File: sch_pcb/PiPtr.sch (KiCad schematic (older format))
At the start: 61 parts, among them J101 GLOBAL_LINK_LEFT, J102 GLOBAL_LINK_RIGHT, J107 RASPBERRY_PI, J111 FP_PIXEL, J112 AM2302, Q101 BSS138, Q102 BSS138, Q103 BSS138, Q104 BSS138, Q105 BSS138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

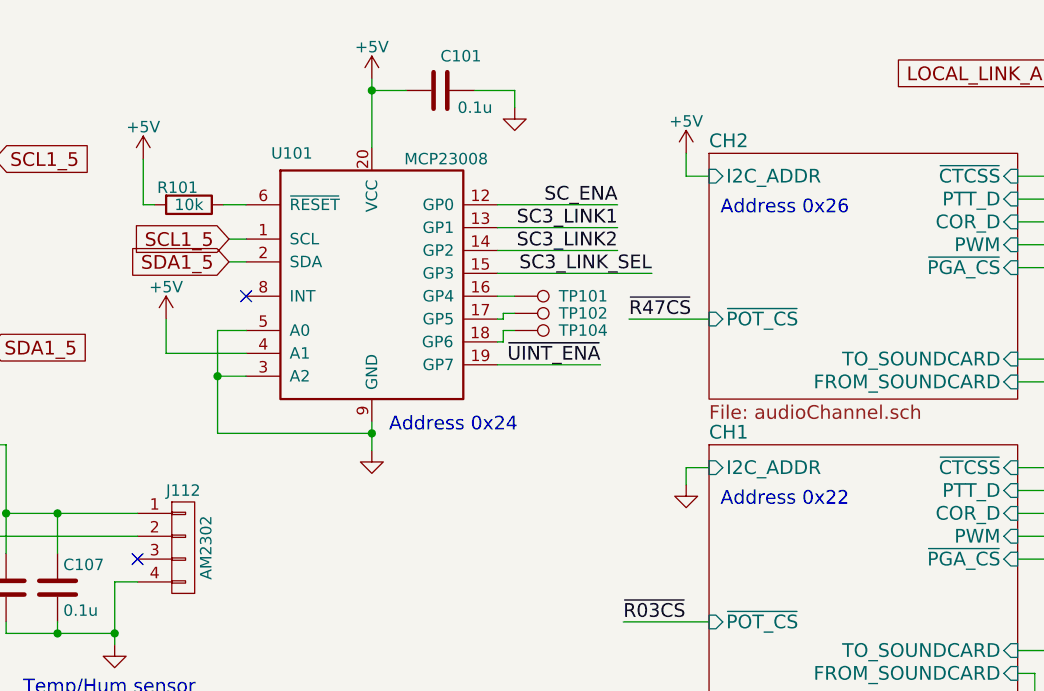
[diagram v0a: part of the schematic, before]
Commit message: Add files via upload
Fix i2c addressing
Change footprint for LDR
Move connectors for temp/hum sensor and rtc so they won't hit the Pi
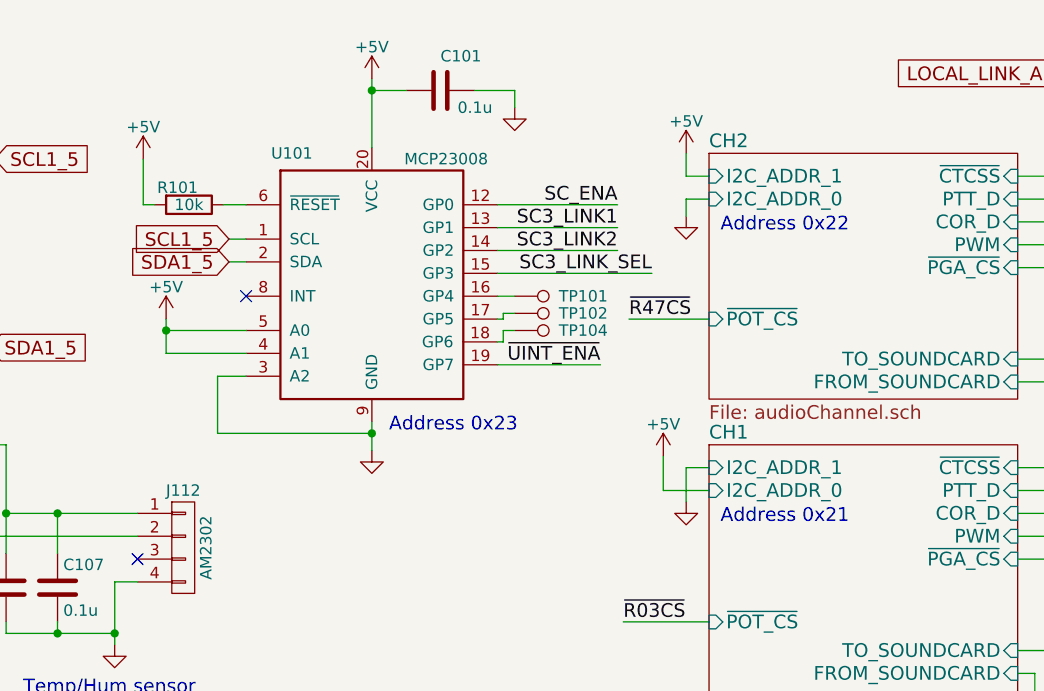
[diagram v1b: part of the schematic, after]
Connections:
- net +5V: now also U101.5 (A0)
- net GND: no longer U101.5 (A0)
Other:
- note added: "Address 0x21"
- note added: "Address 0x23"
- note removed: "Address 0x24"
- note removed: "Address 0x26"
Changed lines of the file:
@@
 F7 "TO_SOUNDCARD" I R 6400 3300 60
 F8 "FROM_SOUNDCARD" I R 6400 3400 60
-F9 "I2C_ADDR" I L 5050 2500 60
-F10 "~POT_CS" I L 5050 3175 60
+F9 "~POT_CS" I L 5050 3175 60
+F10 "I2C_ADDR_1" I L 5050 2500 60
+F11 "I2C_ADDR_0" I L 5050 2600 60
 $EndSheet
 $Sheet
@@
 F7 "TO_SOUNDCARD" I R 6400 2025 60
 F8 "FROM_SOUNDCARD" I R 6400 2125 60
-F9 "I2C_ADDR" I L 5050 1225 60
-F10 "~POT_CS" I L 5050 1850 60
+F9 "~POT_CS" I L 5050 1850 60
+F10 "I2C_ADDR_1" I L 5050 1225 60
+F11 "I2C_ADDR_0" I L 5050 1325 60
 $EndSheet
 $Sheet
@@
 L GND #PWR0128
 U 1 1 596A5C0A
-P 4950 2575
-F 0 "#PWR0128" H 4950 2325 50  0001 C CNN
-F 1 "GND" H 4950 2425 50  0001 C CNN
-F 2 "" H 4950 2575 50  0001 C CNN
-F 3 "" H 4950 2575 50  0001 C CNN
-	1    4950 2575
+P 4950 2650
+F 0 "#PWR0128" H 4950 2400 50  0001 C CNN
+F 1 "GND" H 4950 2500 50  0001 C CNN
+F 2 "" H 4950 2650 50  0001 C CNN
+F 3 "" H 4950 2650 50  0001 C CNN
+	1    4950 2650
 	1    0    0    -1
 $EndComp
@@
 	1    0    0    -1
 $EndComp
-Text Notes 5100 1400 0    60   ~ 0
-Address 0x26
+Text Notes 5100 1475 0    60   ~ 0
+Address 0x22
 Text Label 7875 3025 0    60   ~ 0
 PIXEL_33
@@
 Text GLabel 1900 1975 2    60   Input ~ 0
 SDA1_5
-Text Notes 5100 2675 0    60   ~ 0
-Address 0x22
+Text Notes 5100 2750 0    60   ~ 0
+Address 0x21
 Wire Wire Line
 	4950 1125 4950 1225
@@
 	5050 2500 4950 2500
 Wire Wire Line
-	4950 2500 4950 2575
+	4950 2500 4950 2650
 $Comp
 L R R101
@@
 	2950 1500 3025 1500
 Wire Wire Line
-	2900 1900 2900 2350
-Wire Wire Line
 	2900 2350 3575 2350
 Wire Wire Line
@@
 $EndComp
 Text Notes 3650 2350 0    60   ~ 0
-Address 0x24
+Address 0x23
 Wire Wire Line
 	8775 4075 8125 4075
@@
 Wire Wire Line
 	2675 1850 2675 2000
-Wire Wire Line
-	2900 1900 3025 1900
-Connection ~ 2900 2100
+$Comp
+L +5V #PWR?
+U 1 1 59C8550D
+P 4850 2450
+F 0 "#PWR?" H 4850 2300 50  0001 C CNN
+F 1 "+5V" H 4850 2590 50  0000 C CNN
+F 2 "" H 4850 2450 50  0001 C CNN
+F 3 "" H 4850 2450 50  0001 C CNN
+	1    4850 2450
+	1    0    0    -1
+$EndComp
+Wire Wire Line
+	4850 2450 4850 2600
+Wire Wire Line
+	4850 2600 5050 2600
+Wire Wire Line
+	5050 1325 4950 1325
+Wire Wire Line
+	4950 1325 4950 1400
+$Comp
+L GND #PWR?
+U 1 1 59C85DDE
+P 4950 1400
+F 0 "#PWR?" H 4950 1150 50  0001 C CNN
+F 1 "GND" H 4950 1250 50  0001 C CNN
+F 2 "" H 4950 1400 50  0001 C CNN
+F 3 "" H 4950 1400 50  0001 C CNN
+	1    4950 1400
+	1    0    0    -1
+$EndComp
+Wire Wire Line
+	3025 1900 2675 1900
+Connection ~ 2675 1900
+Wire Wire Line
+	2900 2100 2900 2350
 $EndSCHEMATC

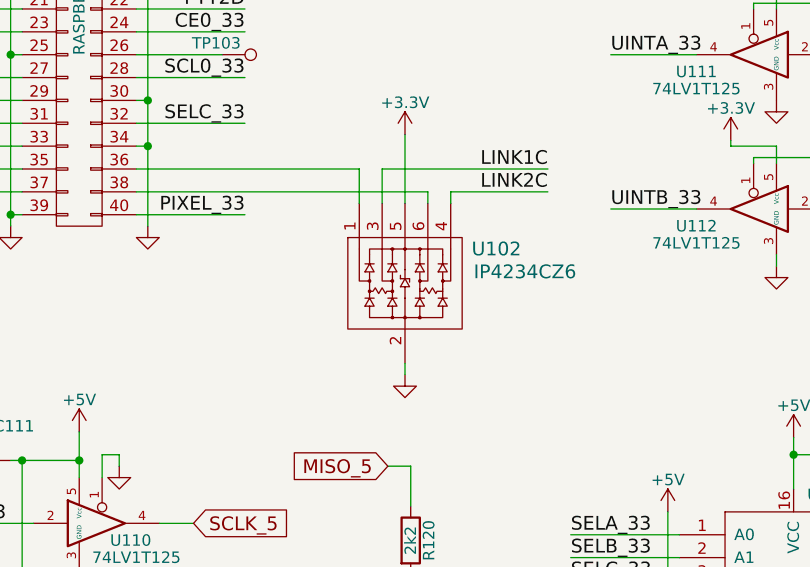
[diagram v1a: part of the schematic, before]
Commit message: Add Digikey part # to all parts.  Fix unconnected nets
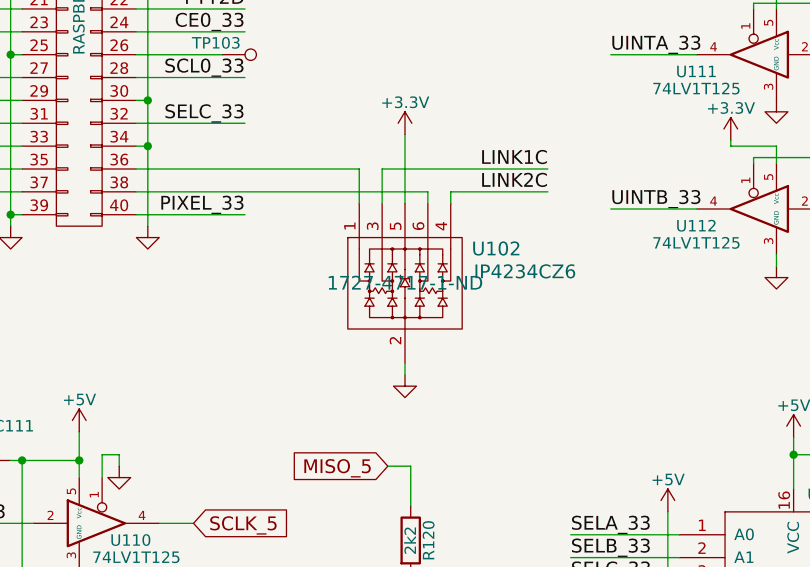
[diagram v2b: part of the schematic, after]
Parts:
- C101, C104, C107, C111, C112: Digikey PN (none) -> 399-1096-1-ND
- C102: Digikey PN (none) -> 399-1061-1-ND
- C103, C106: Digikey PN (none) -> 1276-2087-1-ND
- J101, J102, J111: Digikey PN (none) -> S1012EC-06-ND
- J107: Digikey PN (none) -> SAM10461-ND
- Q102, Q103, Q104, Q105: Digikey PN (none) -> 7-1142-1-ND
- R101, R102, R109, R112, R113: Digikey PN (none) -> 311-10KGRCT-ND
- R103, R117, R123: Digikey PN (none) -> 311-1.0KGRCT-ND
- R104, R105, R107, R110, R111, R114, R120: Digikey PN (none) -> 311-2.2KGRCT-ND
- R106: Digikey PN (none) -> 311-20KGRCT-ND
- R108: Digikey PN (none) -> 311-100KGRCT-ND
- R115, R118: Digikey PN (none) -> 311-33GRCT-ND
- R116, R122: Digikey PN (none) -> 311-3.3KGRCT-ND
- R124: Digikey PN (none) -> 311-100GRCT-ND
- U101: Digikey PN (none) -> MCP23008-E/SS-ND
- U102: Digikey PN (none) -> 1727-4717-1-ND
- U104: Digikey PN (none) -> 296-14863-1-ND
- U105, U110, U111, U112, U113: Digikey PN (none) -> 96-37172-1-ND
- U106: Digikey PN (none) -> MCP6004-I/SL-ND
- U108: Digikey PN (none) -> 1727-6368-1-ND
- U109: Digikey PN (none) -> 296-14908-1-ND
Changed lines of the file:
@@
 F 2 "lib:RaspberryPi2x20" H 1375 3475 50  0001 C CNN
 F 3 "" H 1375 3475 50  0001 C CNN
+F 4 "SAM10461-ND" H 1375 3475 50  0001 C CNN "Digikey PN"
 	1    1375 4425
 	1    0    0    -1
@@
 F 2 "lib:SOT23" H 8500 2100 50  0001 L CIN
 F 3 "" H 8300 2175 50  0001 L CNN
+F 4 "7-1142-1-ND" H 8300 2175 50  0001 L CNN "Digikey PN"
 	1    8300 2175
 	1    0    0    -1
@@
 F 2 "lib:smd0603" V 2755 6800 50  0001 C CNN
 F 3 "" H 2825 6800 50  0001 C CNN
+F 4 "311-2.2KGRCT-ND" H 2825 6800 50  0001 C CNN "Digikey PN"
 	1    2825 6800
 	1    0    0    -1
@@
 F 2 "lib:smd0603" V 2755 7200 50  0001 C CNN
 F 3 "" H 2825 7200 50  0001 C CNN
+F 4 "311-3.3KGRCT-ND" H 2825 7200 50  0001 C CNN "Digikey PN"
 	1    2825 7200
 	1    0    0    -1
@@
 F 2 "lib:SIL-3" H 9625 3025 50  0001 C CNN
 F 3 "" H 9625 3025 50  0001 C CNN
+F 4 "S1012EC-06-ND" H 9625 3025 50  0001 C CNN "Digikey PN"
 	1    9625 3025
 	1    0    0    -1
@@
 F 2 "lib:SOT23" H 1500 975 50  0001 L CIN
 F 3 "" H 1300 1050 50  0001 L CNN
-F 4 "7-1142-1-ND" V 1300 1050 60  0001 C CNN "Digikey PN"
+F 4 "7-1142-1-ND" V 1300 1050 60  0001 L CNN "Digikey PN"
 	1    1300 1050
 	0    1    1    0
@@
 F 2 "lib:smd0603" V 980 950 50  0001 C CNN
 F 3 "" H 1050 950 50  0001 C CNN
+F 4 "311-2.2KGRCT-ND" H 1050 950 50  0001 C CNN "Digikey PN"
 	1    1050 950
 	1    0    0    -1
@@
 F 2 "lib:smd0603" V 1480 950 50  0001 C CNN
 F 3 "" H 1550 950 50  0001 C CNN
+F 4 "311-2.2KGRCT-ND" H 1550 950 50  0001 C CNN "Digikey PN"
 	1    1550 950
 	1    0    0    -1
@@
 F 2 "lib:SOT23" H 9750 2100 50  0001 L CIN
 F 3 "" H 9550 2175 50  0001 L CNN
+F 4 "7-1142-1-ND" H 9550 2175 50  0001 L CNN "Digikey PN"
 	1    9550 2175
 	1    0    0    -1
@@
 F 2 "lib:SOT23" H 1475 1800 50  0001 L CIN
 F 3 "" H 1275 1875 50  0001 L CNN
+F 4 "7-1142-1-ND" H 1275 1875 50  0001 L CNN "Digikey PN"
 	1    1275 1875
 	0    1    1    0
@@
 F 2 "lib:smd0603" V 955 1775 50  0001 C CNN
 F 3 "" H 1025 1775 50  0001 C CNN
+F 4 "311-2.2KGRCT-ND" H 1025 1775 50  0001 C CNN "Digikey PN"
 	1    1025 1775
 	1    0    0    -1
@@
 F 2 "lib:smd0603" V 1455 1775 50  0001 C CNN
 F 3 "" H 1525 1775 50  0001 C CNN
+F 4 "311-2.2KGRCT-ND" H 1525 1775 50  0001 C CNN "Digikey PN"
 	1    1525 1775
 	1    0    0    -1
@@
 F 2 "lib:smd0603" V 1680 2400 50  0001 C CNN
 F 3 "" H 1750 2400 50  0001 C CNN
+F 4 "311-33GRCT-ND" H 1750 2400 50  0001 C CNN "Digikey PN"
 	1    1750 2400
 	0    1    1    0
@@
 F 2 "lib:smd0603" H 2013 2875 50  0001 C CNN
 F 3 "" H 1975 3025 50  0001 C CNN
+F 4 "1276-2087-1-ND" H 1975 3025 50  0001 C CNN "Digikey PN"
 	1    1975 3025
 	1    0    0    -1
@@
 F 2 "lib:smd0603" H 2238 2875 50  0001 C CNN
 F 3 "" H 2200 3025 50  0001 C CNN
+F 4 "399-1096-1-ND" H 2200 3025 50  0001 C CNN "Digikey PN"
 	1    2200 3025
 	1    0    0    -1
@@
 F 2 "lib:SOT23" H 1450 2625 50  0001 L CIN
 F 3 "" H 1250 2700 50  0001 L CNN
+F 4 "7-1142-1-ND" H 1250 2700 50  0001 L CNN "Digikey PN"
 	1    1250 2700
 	0    1    1    0
@@
 F 2 "lib:smd0603" V 930 2600 50  0001 C CNN
 F 3 "" H 1000 2600 50  0001 C CNN
+F 4 "311-10KGRCT-ND" H 1000 2600 50  0001 C CNN "Digikey PN"
 	1    1000 2600
 	1    0    0    -1
@@
 F 2 "lib:smd0603" V 1430 2600 50  0001 C CNN
 F 3 "" H 1500 2600 50  0001 C CNN
+F 4 "311-10KGRCT-ND" H 1500 2600 50  0001 C CNN "Digikey PN"
 	1    1500 2600
 	1    0    0    -1
@@
 F 2 "lib:SOIC16" H 4500 7125 50  0001 C CNN
 F 3 "" H 4500 7125 50  0001 C CNN
+F 4 "296-14863-1-ND" H 4500 7125 50  0001 C CNN "Digikey PN"
 	1    4500 7125
 	1    0    0    -1
@@
 F 2 "lib:smd0603" H 4813 6275 50  0001 C CNN
 F 3 "" H 4775 6425 50  0001 C CNN
+F 4 "399-1096-1-ND" H 4775 6425 50  0001 C CNN "Digikey PN"
 	1    4775 6425
 	0    1    1    0
@@
 F 2 "lib:smd0603" V 9080 3025 50  0001 C CNN
 F 3 "" H 9150 3025 50  0001 C CNN
+F 4 "311-100GRCT-ND" H 9150 3025 50  0001 C CNN "Digikey PN"
 	1    9150 3025
 	0    1    1    0
@@
 F 2 "lib:SOT23-6" H 2800 5675 60  0001 C CNN
 F 3 "" H 2800 5675 60  0000 C CNN
+F 4 "1727-4717-1-ND" H 2800 5675 60  0000 C CNN "Digikey PN"
 	1    2800 5675
 	1    0    0    -1
@@
 F 2 "lib:smd0603" V 6855 775 50  0001 C CNN
 F 3 "" H 6925 775 50  0001 C CNN
+F 4 "311-1.0KGRCT-ND" H 6925 775 50  0001 C CNN "Digikey PN"
 	1    6925 775
 	0    1    1    0
@@
 F 2 "lib:SOT23-5" H 8625 3025 50  0001 C CNN
 F 3 "" H 8625 3025 50  0001 C CNN
+F 4 "96-37172-1-ND" H 8625 3025 50  0001 C CNN "Digikey PN"
 	1    8625 3025
 	1    0    0    -1
@@
 F 2 "lib:SOT23-5" H 4325 4675 50  0001 C CNN
 F 3 "" H 4325 4675 50  0001 C CNN
+F 4 "96-37172-1-ND" H 4325 4675 50  0001 C CNN "Digikey PN"
 	1    4325 4675
 	-1   0    0    -1
@@
 F 2 "lib:SOT23-5" H 4325 5350 50  0001 C CNN
 F 3 "" H 4325 5350 50  0001 C CNN
+F 4 "96-37172-1-ND" H 4325 5350 50  0001 C CNN "Digikey PN"
 	1    4325 5350
 	-1   0    0    -1
@@
 F 2 "lib:SIL-6" H 8450 1250 50  0001 C CNN
 F 3 "" H 8450 1250 50  0001 C CNN
+F 4 "S1012EC-06-ND" H 8450 1250 50  0001 C CNN "Digikey PN"
 	1    8450 1250
 	1    0    0    -1
@@
 F 2 "lib:SIL-6" H 9725 1250 50  0001 C CNN
 F 3 "" H 9725 1250 50  0001 C CNN
+F 4 "S1012EC-06-ND" H 9725 1250 50  0001 C CNN "Digikey PN"
 	1    9725 1250
 	1    0    0    -1
@@
 F 2 "lib:SOT23-5" H 1475 6725 50  0001 C CNN
 F 3 "" H 1475 6725 50  0001 C CNN
+F 4 "96-37172-1-ND" H 1475 6725 50  0001 C CNN "Digikey PN"
 	1    1475 6725
 	1    0    0    -1
@@
 F 2 "lib:SOT23-5" H 1475 7400 50  0001 C CNN
 F 3 "" H 1475 7400 50  0001 C CNN
+F 4 "96-37172-1-ND" H 1475 7400 50  0001 C CNN "Digikey PN"
 	1    1475 7400
 	1    0    0    -1
@@
 F 2 "lib:smd0603" H 963 6300 50  0001 C CNN
 F 3 "" H 925 6450 50  0001 C CNN
+F 4 "399-1096-1-ND" H 925 6450 50  0001 C CNN "Digikey PN"
 	1    925  6450
 	0    1    1    0
@@
 F 2 "lib:SOIC14" H 7650 4025 50  0001 C CNN
 F 3 "" H 7750 4125 50  0001 C CNN
+F 4 "MCP6004-I/SL-ND" H 7750 4125 50  0001 C CNN "Digikey PN"
 	2    7700 3925
 	1    0    0    -1
@@
 F 2 "lib:smd0603" H 7588 4375 50  0001 C CNN
 F 3 "" H 7550 4525 50  0001 C CNN
+F 4 "399-1061-1-ND" H 7550 4525 50  0001 C CNN "Digikey PN"
 	1    7550 4525
 	0    1    1    0
@@
 F 2 "lib:smd0603" V 7480 4325 50  0001 C CNN
 F 3 "" H 7550 4325 50  0001 C CNN
+F 4 "311-100KGRCT-ND" H 7550 4325 50  0001 C CNN "Digikey PN"
 	1    7550 4325
 	0    1    1    0
@@
 F 2 "lib:smd0603" V 7130 4375 50  0001 C CNN
 F 3 "" H 7200 4375 50  0001 C CNN
+F 4 "311-10KGRCT-ND" H 7200 4375 50  0001 C CNN "Digikey PN"
 	1    7200 4375
 	1    0    0    -1
@@
 F 2 "lib:smd0603" V 6980 3825 50  0001 C CNN
 F 3 "" H 7050 3825 50  0001 C CNN
+F 4 "311-1.0KGRCT-ND" H 7050 3825 50  0001 C CNN "Digikey PN"
 	1    7050 3825
 	0    1    1    0
@@
 F 2 "lib:smd0603" V 8305 3925 50  0001 C CNN
 F 3 "" H 8375 3925 50  0001 C CNN
+F 4 "311-20KGRCT-ND" H 8375 3925 50  0001 C CNN "Digikey PN"
 	1    8375 3925
 	0    1    1    0
@@
 F 2 "lib:smd0603" V 7230 3550 50  0001 C CNN
 F 3 "" H 7300 3550 50  0001 C CNN
+F 4 "311-10KGRCT-ND" H 7300 3550 50  0001 C CNN "Digikey PN"
 	1    7300 3550
 	1    0    0    -1
@@
 F 2 "lib:smd0603" V 9555 3925 50  0001 C CNN
 F 3 "" H 9625 3925 50  0001 C CNN
+F 4 "311-2.2KGRCT-ND" H 9625 3925 50  0001 C CNN "Digikey PN"
 	1    9625 3925
 	0    1    1    0
@@
 F 2 "lib:smd0603" V 9555 4500 50  0001 C CNN
 F 3 "" H 9625 4500 50  0001 C CNN
+F 4 "311-2.2KGRCT-ND" H 9625 4500 50  0001 C CNN "Digikey PN"
 	1    9625 4500
 	0    1    1    0
@@
 F 2 "lib:SOIC14" H 9175 3676 60  0001 C CNN
 F 3 "" H 9075 3925 60  0001 C CNN
+F 4 "1727-6368-1-ND" H 9075 3925 60  0001 C CNN "Digikey PN"
 	1    9075 3925
 	1    0    0    -1
@@
 F 2 "lib:SOIC14" H 9175 4251 60  0001 C CNN
 F 3 "" H 9075 4500 60  0001 C CNN
+F 4 "1727-6368-1-ND" H 9075 4500 60  0001 C CNN "Digikey PN"
 	2    9075 4500
 	1    0    0    -1
@@
 F 2 "lib:SOT23-6" H 8425 5675 50  0001 C CNN
 F 3 "" H 8425 5675 50  0001 C CNN
+F 4 "296-14908-1-ND" H 8425 5675 50  0001 C CNN "Digikey PN"
 	1    8425 5675
 	-1   0    0    -1
@@
 F 2 "lib:SOIC14" H 9075 5875 50  0001 C CNN
 F 3 "" H 9175 5975 50  0001 C CNN
+F 4 "MCP6004-I/SL-ND" H 9175 5975 50  0001 C CNN "Digikey PN"
 	1    9125 5775
 	1    0    0    -1
@@
 F 2 "lib:smd0603" H 8588 5150 50  0001 C CNN
 F 3 "" H 8550 5300 50  0001 C CNN
+F 4 "1276-2087-1-ND" H 8550 5300 50  0001 C CNN "Digikey PN"
 	1    8550 5300
 	1    0    0    -1
@@
 F 2 "lib:smd0603" H 8838 5150 50  0001 C CNN
 F 3 "" H 8800 5300 50  0001 C CNN
+F 4 "399-1096-1-ND" H 8800 5300 50  0001 C CNN "Digikey PN"
 	1    8800 5300
 	1    0    0    -1
@@
 F 2 "lib:smd0603" V 8230 5050 50  0001 C CNN
 F 3 "" H 8300 5050 50  0001 C CNN
+F 4 "311-33GRCT-ND" H 8300 5050 50  0001 C CNN "Digikey PN"
 	1    8300 5050
 	0    1    1    0
@@
 F 2 "lib:smd0603" V 9605 5775 50  0001 C CNN
 F 3 "" H 9675 5775 50  0001 C CNN
+F 4 "311-3.3KGRCT-ND" H 9675 5775 50  0001 C CNN "Digikey PN"
 	1    9675 5775
 	0    1    1    0
@@
 F 2 "lib:smd0603" V 10055 5775 50  0001 C CNN
 F 3 "" H 10125 5775 50  0001 C CNN
+F 4 "311-1.0KGRCT-ND" H 10125 5775 50  0001 C CNN "Digikey PN"
 	1    10125 5775
 	0    -1   -1   0
@@
 F 2 "lib:smd0603" V 2705 1350 50  0001 C CNN
 F 3 "" H 2775 1350 50  0001 C CNN
+F 4 "311-10KGRCT-ND" H 2775 1350 50  0001 C CNN "Digikey PN"
 	1    2775 1350
 	0    1    1    0
@@
 F 2 "lib:smd0603" H 3913 700 50  0001 C CNN
 F 3 "" H 3875 850 50  0001 C CNN
+F 4 "399-1096-1-ND" H 3875 850 50  0001 C CNN "Digikey PN"
 	1    3875 850
 	0    1    1    0
@@
 F 2 "lib:SSOP-20" H 3625 750 50  0001 L CNN
 F 3 "" H 3825 2700 50  0001 C CNN
+F 4 "MCP23008-E/SS-ND" H 3825 2700 50  0001 C CNN "Digikey PN"
 	1    3575 1700
 	1    0    0    -1
@@
 	2675 1850 2675 2000
 $Comp
-L +5V #PWR?
+L +5V #PWR03
 U 1 1 59C8550D
 P 4850 2450
-F 0 "#PWR?" H 4850 2300 50  0001 C CNN
+F 0 "#PWR03" H 4850 2300 50  0001 C CNN
 F 1 "+5V" H 4850 2590 50  0000 C CNN
 F 2 "" H 4850 2450 50  0001 C CNN
@@
 	4950 1325 4950 1400
 $Comp
-L GND #PWR?
+L GND #PWR04
 U 1 1 59C85DDE
 P 4950 1400
-F 0 "#PWR?" H 4950 1150 50  0001 C CNN
+F 0 "#PWR04" H 4950 1150 50  0001 C CNN
 F 1 "GND" H 4950 1250 50  0001 C CNN
 F 2 "" H 4950 1400 50  0001 C CNN

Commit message: Switch to 0402 parts and SeeedStudio footprints
Silk screen is still being updated.  BOM needs to be updated as well
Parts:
- C101, C102, C103, C104, C106, C107, C111, C112: footprint lib:smd0603 -> lib:OPL_C0402
- J101, J102: footprint lib:SIL-6 -> lib:OPL_H6-2.54
- J111: footprint lib:SIL-3 -> lib:OPL_H3-2.54
- J112: footprint lib:SIL-4 -> lib:OPL_H4-2.54
- Q101, Q102, Q103, Q104, Q105: footprint lib:SOT23 -> lib:OPL_SOT-23
- R101, R102, R103, R104, R105, R106, R107, R108, R109, R110, R111, R112, R113, R114, R115, R116, R117, R118, R120, R122, R123, R124: footprint lib:smd0603 -> lib:OPL_R0402
- U101: footprint lib:SSOP-20 -> lib:OPL_TSSOP20-0.65-6.5X4.4MM
- U102, U109: footprint lib:SOT23-6 -> lib:OPL_SOT-23-6
- U105, U110, U111, U112, U113: footprint lib:SOT23-5 -> lib:OPL_SOT-23-5
